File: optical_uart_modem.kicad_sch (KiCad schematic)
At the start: 9 parts, among them J1 Conn_01x06_Male, Q1 KT315, Q2 Q_Photo_NPN, Q4 FDN337N, U1 74HC08

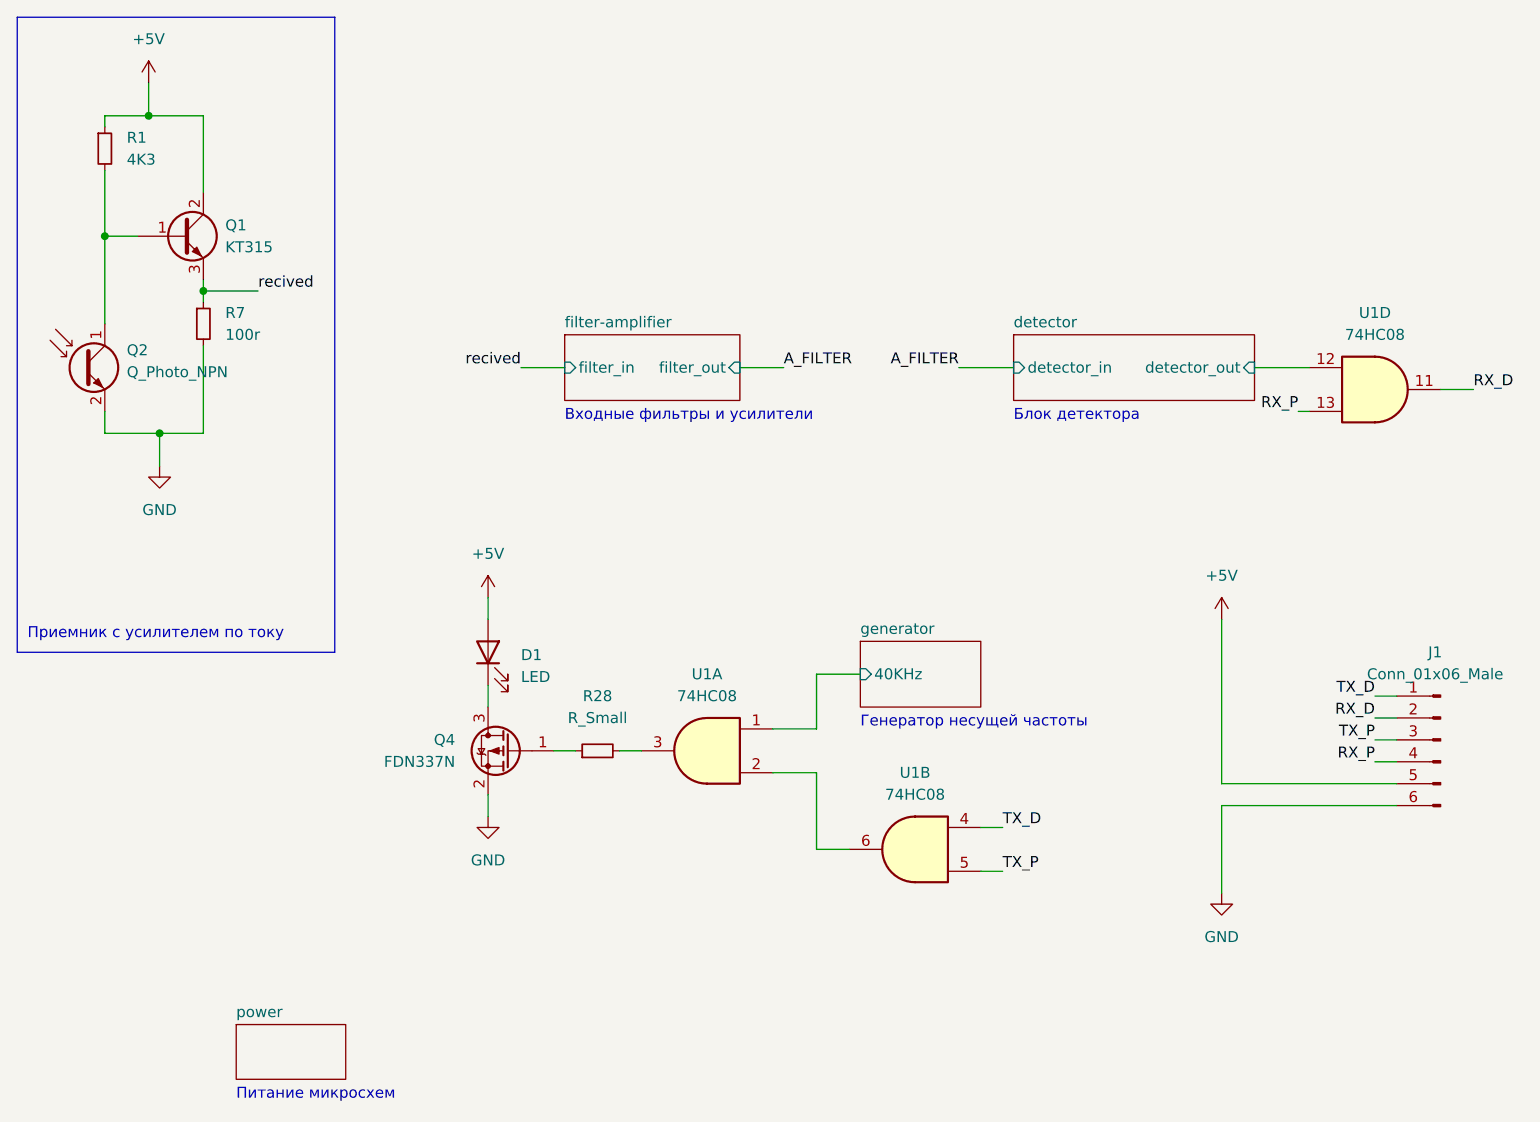
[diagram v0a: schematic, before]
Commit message: test points and some silk added
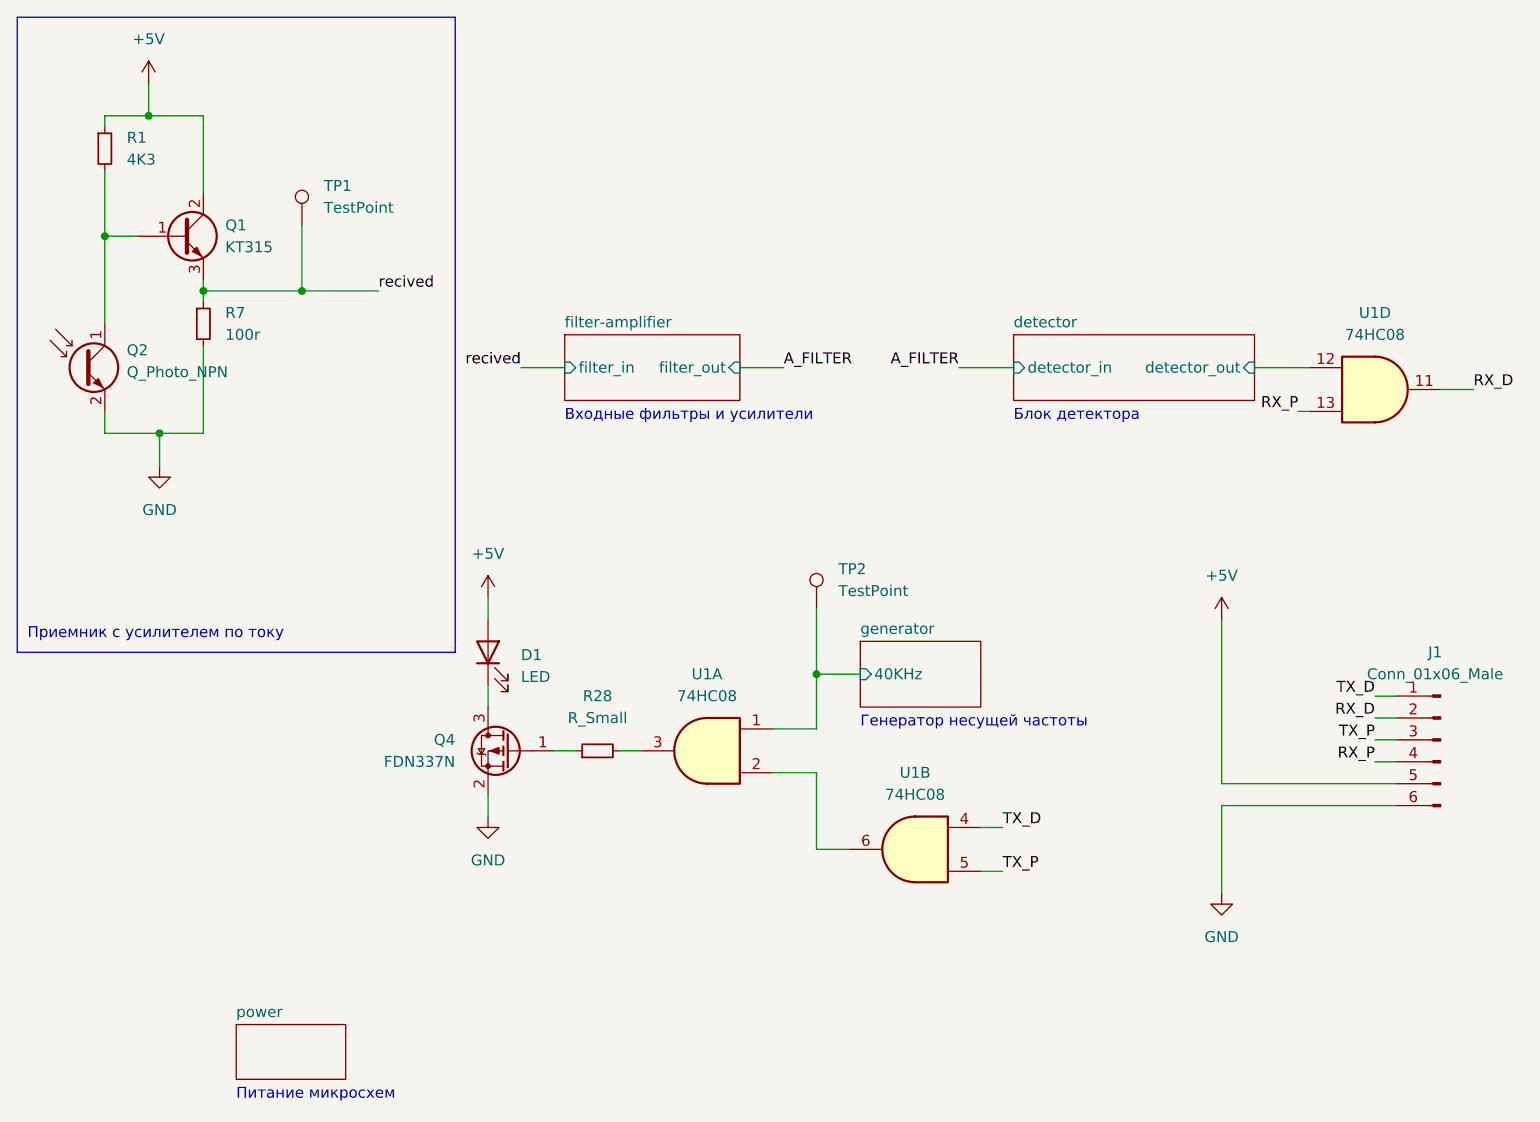
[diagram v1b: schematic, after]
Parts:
- added TP1, TP2: TestPoint, TestPoint:TestPoint_Pad_D1.0mm, symbol Connector:TestPoint
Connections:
- net generator/40KHz: now also TP2.1
- net recived: now also TP1.1
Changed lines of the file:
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@@
   (junction (at 55.88 60.96) (diameter 0) (color 0 0 0 0)
   )
+  (junction (at 138.43 111.76) (diameter 0) (color 0 0 0 0)
+  )
   (junction (at 67.31 67.31) (diameter 0) (color 0 0 0 0)
   )
+  (junction (at 78.74 67.31) (diameter 0) (color 0 0 0 0)
+  )
   (wire (pts (xy 59.69 60.96) (xy 55.88 60.96))
     (stroke (width 0) (type default) (color 0 0 0 0))
   )
-  (polyline (pts (xy 82.55 35.56) (xy 82.55 109.22))
+  (polyline (pts (xy 96.52 35.56) (xy 96.52 109.22))
     (stroke (width 0) (type default) (color 0 0 0 0))
   )
@@
     (stroke (width 0) (type default) (color 0 0 0 0))
   )
-  (wire (pts (xy 67.31 67.31) (xy 73.66 67.31))
+  (wire (pts (xy 67.31 67.31) (xy 78.74 67.31))
     (stroke (width 0) (type default) (color 0 0 0 0))
   )
@@
     (stroke (width 0) (type default) (color 0 0 0 0))
   )
-  (polyline (pts (xy 45.72 109.22) (xy 82.55 109.22))
+  (polyline (pts (xy 45.72 109.22) (xy 96.52 109.22))
     (stroke (width 0) (type default) (color 0 0 0 0))
   )
@@
     (stroke (width 0) (type default) (color 0 0 0 0))
   )
+  (wire (pts (xy 78.74 59.69) (xy 78.74 67.31))
+    (stroke (width 0) (type default) (color 0 0 0 0))
+  )
   (wire (pts (xy 62.23 83.82) (xy 67.31 83.82))
     (stroke (width 0) (type default) (color 0 0 0 0))
@@
     (stroke (width 0) (type default) (color 0 0 0 0))
   )
+  (wire (pts (xy 138.43 104.14) (xy 138.43 111.76))
+    (stroke (width 0) (type default) (color 0 0 0 0))
+  )
   (wire (pts (xy 154.94 76.2) (xy 161.29 76.2))
     (stroke (width 0) (type default) (color 0 0 0 0))
@@
     (stroke (width 0) (type default) (color 0 0 0 0))
   )
-  (polyline (pts (xy 82.55 35.56) (xy 45.72 35.56))
+  (polyline (pts (xy 96.52 35.56) (xy 45.72 35.56))
     (stroke (width 0) (type default) (color 0 0 0 0))
   )
@@
   )
   (wire (pts (xy 100.33 102.87) (xy 100.33 105.41))
+    (stroke (width 0) (type default) (color 0 0 0 0))
+  )
+  (wire (pts (xy 78.74 67.31) (xy 87.63 67.31))
     (stroke (width 0) (type default) (color 0 0 0 0))
   )
@@
     (effects (font (size 1.27 1.27)) (justify right bottom))
   )
-  (label "recived" (at 73.66 67.31 0)
+  (label "recived" (at 87.63 67.31 0)
     (effects (font (size 1.27 1.27)) (justify left bottom))
   )
@@
     )
     (property "Datasheet" "" (id 3) (at 60.96 43.18 0)
+      (effects (font (size 1.27 1.27)) hide)
+    )
+    (pin "1")
+  )
+  (symbol (lib_id "Connector:TestPoint") (at 138.43 104.14 0) (unit 1)
+    (in_bom yes) (on_board yes) (fields_autoplaced)
+    (property "Reference" "TP2" (id 0) (at 140.97 99.5679 0)
+      (effects (font (size 1.27 1.27)) (justify left))
+    )
+    (property "Value" "TestPoint" (id 1) (at 140.97 102.1079 0)
+      (effects (font (size 1.27 1.27)) (justify left))
+    )
+    (property "Footprint" "TestPoint:TestPoint_Pad_D1.0mm" (id 2) (at 143.51 104.14 0)
+      (effects (font (size 1.27 1.27)) hide)
+    )
+    (property "Datasheet" "~" (id 3) (at 143.51 104.14 0)
       (effects (font (size 1.27 1.27)) hide)
     )
@@
     (pin "1")
     (pin "2")
+  )
+  (symbol (lib_id "Connector:TestPoint") (at 78.74 59.69 0) (unit 1)
+    (in_bom yes) (on_board yes) (fields_autoplaced)
+    (property "Reference" "TP1" (id 0) (at 81.28 55.1179 0)
+      (effects (font (size 1.27 1.27)) (justify left))
+    )
+    (property "Value" "TestPoint" (id 1) (at 81.28 57.6579 0)
+      (effects (font (size 1.27 1.27)) (justify left))
+    )
+    (property "Footprint" "TestPoint:TestPoint_Pad_D1.0mm" (id 2) (at 83.82 59.69 0)
+      (effects (font (size 1.27 1.27)) hide)
+    )
+    (property "Datasheet" "~" (id 3) (at 83.82 59.69 0)
+      (effects (font (size 1.27 1.27)) hide)
+    )
+    (pin "1")
   )
   (symbol (lib_id "Device:R_Small") (at 55.88 50.8 0) (unit 1)
@@
       (reference "RV4") (unit 1) (value "74K") (footprint "Potentiometer_THT:Potentiometer_Bourns_3296W_Vertical")
     )
+    (path "/c824a5e3-df89-44cd-8628-dfb590cfba5c"
+      (reference "TP1") (unit 1) (value "TestPoint") (footprint "TestPoint:TestPoint_Pad_D1.0mm")
+    )
+    (path "/179ded49-c8d7-40c2-a728-5841fda625bd"
+      (reference "TP2") (unit 1) (value "TestPoint") (footprint "TestPoint:TestPoint_Pad_D1.0mm")
+    )
+    (path "/922bae2e-bcad-4760-a906-21dea416b5dc/126ccd0e-610f-4fa4-8021-30873a398967"
+      (reference "TP3") (unit 1) (value "TestPoint") (footprint "TestPoint:TestPoint_Pad_D1.0mm")
+    )
+    (path "/922bae2e-bcad-4760-a906-21dea416b5dc/90872d08-1d12-472c-928b-b8ba166eab5b"
+      (reference "TP4") (unit 1) (value "TestPoint") (footprint "TestPoint:TestPoint_Pad_D1.0mm")
+    )
+    (path "/4d9c5bb1-1a0b-4685-9b64-9623bdfa6e36/6474c344-9c49-4bfa-864c-4de08282c068"
+      (reference "TP5") (unit 1) (value "TestPoint") (footprint "TestPoint:TestPoint_Pad_D1.0mm")
+    )
+    (path "/4d9c5bb1-1a0b-4685-9b64-9623bdfa6e36/b9897f60-9679-49ed-b35b-04f4fc598fe6"
+      (reference "TP6") (unit 1) (value "TestPoint") (footprint "TestPoint:TestPoint_Pad_D1.0mm")
+    )
     (path "/f914a7f8-67aa-42b4-8ceb-a268a2199523"

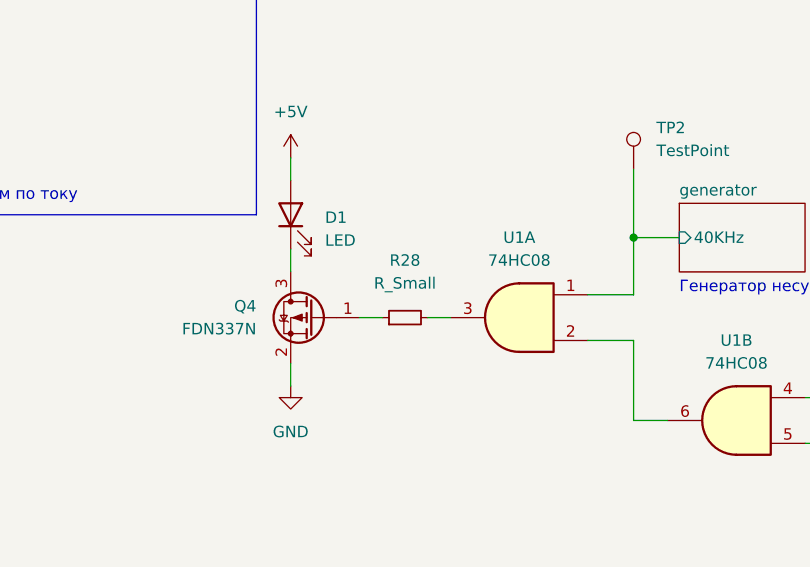
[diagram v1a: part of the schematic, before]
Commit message: polygons error fixed
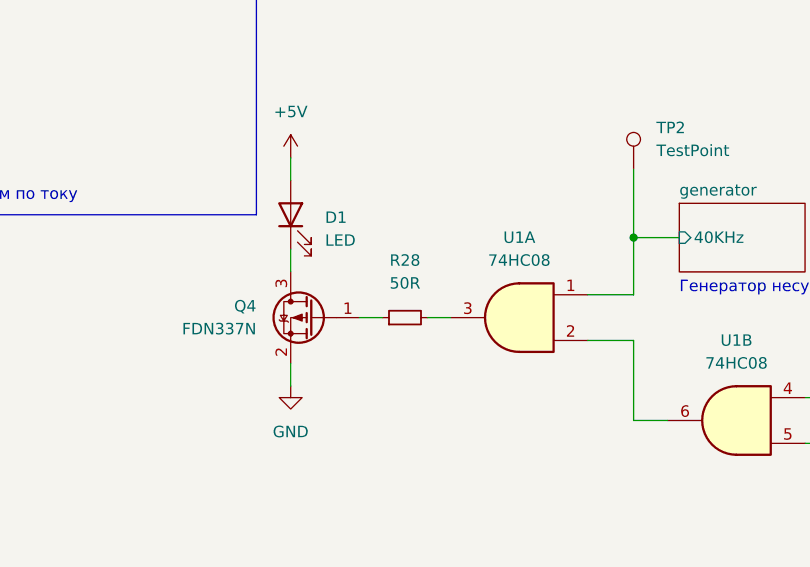
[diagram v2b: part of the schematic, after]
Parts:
- R28: value R_Small -> 50R
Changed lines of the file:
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@@
     (in_bom yes) (on_board yes) (fields_autoplaced)
     (property "Reference" "R28" (id 0) (at 113.03 114.3 90))
-    (property "Value" "R_Small" (id 1) (at 113.03 116.84 90))
+    (property "Value" "50R" (id 1) (at 113.03 116.84 90))
     (property "Footprint" "Resistor_SMD:R_0603_1608Metric" (id 2) (at 113.03 120.65 0)
       (effects (font (size 1.27 1.27)) hide)
@@
     )
     (path "/e28785e6-23a6-4d97-8af1-f33c992f70f8/b3b988cb-e491-4498-a4b7-d91f969f3ea5"
-      (reference "C17") (unit 1) (value "C_Small") (footprint "Capacitor_SMD:C_0603_1608Metric")
+      (reference "C17") (unit 1) (value "0.47n") (footprint "Capacitor_SMD:C_0603_1608Metric")
     )
     (path "/e28785e6-23a6-4d97-8af1-f33c992f70f8/badacdf9-a514-4360-9eb6-46665e85c9e6"
-      (reference "C18") (unit 1) (value "C_Small") (footprint "Capacitor_SMD:C_0603_1608Metric")
+      (reference "C18") (unit 1) (value "0.01u") (footprint "Capacitor_SMD:C_0603_1608Metric")
     )
     (path "/705194a5-b853-4555-b7f4-2e5e82a735a9"
@@
     )
     (path "/e28785e6-23a6-4d97-8af1-f33c992f70f8/c45d9a51-8025-41b1-82d8-34e2a8fd0ca0"
-      (reference "R26") (unit 1) (value "R_Small") (footprint "Resistor_SMD:R_0603_1608Metric")
+      (reference "R26") (unit 1) (value "560K") (footprint "Resistor_SMD:R_0603_1608Metric")
     )
     (path "/e28785e6-23a6-4d97-8af1-f33c992f70f8/cfca1c89-e531-48ad-aa93-3666292446e4"
-      (reference "R27") (unit 1) (value "R_Small") (footprint "Resistor_SMD:R_0603_1608Metric")
+      (reference "R27") (unit 1) (value "39K") (footprint "Resistor_SMD:R_0603_1608Metric")
     )
     (path "/c617335c-bbb9-4ba2-bf32-96285610c756"
-      (reference "R28") (unit 1) (value "R_Small") (footprint "Resistor_SMD:R_0603_1608Metric")
+      (reference "R28") (unit 1) (value "50R") (footprint "Resistor_SMD:R_0603_1608Metric")
     )
     (path "/922bae2e-bcad-4760-a906-21dea416b5dc/93afe5b9-ac56-4aea-8798-699080b634cf"
